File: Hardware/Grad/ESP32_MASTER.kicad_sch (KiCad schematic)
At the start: 35 parts, among them J201 Amphenol 40-Pin FPC, U201 LM66200DRLR, U202 TLV75733PDRV, U203 SN74LVC1G139, U204 ESP32-S3-WROOM-1-N8R8, U205 TC7MBL3126CFT, U206 AP3019AKTTR, U207 W25Q128JVP, U208 THVD1400D

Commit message: Prototype of PCB layout
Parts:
- added C1101, C1104, C1105: 100nF, Capacitor_SMD:C_0402_1005Metric, symbol Device:C_Small_US
- added C1102, C1103, C1106: 22uF, Capacitor_SMD:C_0603_1608Metric, symbol Device:C_Polarized_Small_US
- added D1101, D1102: LED_Small, New_Library:Worthington_LED_0603, symbol Device:LED_Small
- added J101: 6-Pos 2.54mm Header, Connector_PinHeader_2.54mm:PinHeader_1x06_P2.54mm_Vertical_SMD_Pin1Left, symbol Connector_Generic:Conn_01x06
- added J1101: JST-PH SPI, Connector_JST:JST_PH_S5B-PH-K_1x05_P2.00mm_Horizontal, symbol Connector_Generic:Conn_01x05
- added J1102: JST-PH UART/I2C, Connector_JST:JST_PH_S6B-PH-K_1x06_P2.00mm_Horizontal, symbol Connector_Generic:Conn_01x06
- added J1103: JST-PH A#, Connector_JST:JST_PH_S6B-PH-K_1x06_P2.00mm_Horizontal, symbol Connector_Generic:Conn_01x06
- added J1104: Micro_SD_Card, New_Library:CUI_MSD-4-A, symbol Connector:Micro_SD_Card
- added J202, J203, J204, J205: 01x30 Pads, Connector_PinSocket_2.54mm:PinSocket_1x30_P2.54mm_Vertical, symbol Connector_Generic:Conn_01x30
- added J3: 2x8 2.54mm IDC Header, Connector_IDC:IDC-Header_2x06_P2.54mm_Vertical_SMD, symbol Connector_Generic:Conn_02x06_Odd_Even
- added R1101: 1k, New_Library:Worthington_R_0402, symbol Device:R_Small_US
- added R1102: 430, New_Library:Worthington_R_0402, symbol Device:R_Small_US
- added R203, R204: 120, New_Library:Worthington_R_0402, symbol Device:R_Small_US
- added RN1101: 47k, New_Library:RESCAXE80P320X160X70-8N, symbol Libraries:R_Network04_Split
- added U1101: TC7MBL3126CFT, Package_SO:TSSOP-14_4.4x5mm_P0.65mm, symbol Analog_Switch:CD4066BPW
- added U1102: AZ1117-5.0, Package_TO_SOT_SMD:SOT-223-3_TabPin2, symbol Regulator_Linear:AZ1117-5.0
- added U1103: THVD1400D, Package_SO:SOIC-8_3.9x4.9mm_P1.27mm, symbol Interface_UART:THVD1400D
- added U1104: QTPy SAMD21, New_Library:Py_QT_SAMD21, symbol New_Library:QT_Py_SAMD21
- D201: value LED_Small -> RED
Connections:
- net BACKLIGHT_PWM_IN: now also J3.8 (Pin_8)
- net BATT_IN: now also C1102.1, J3.1 (Pin_1), J3.12 (Pin_12), U1102.3 (VI)
- net ESP_PROG_EN: now also J101.2 (Pin_2)
- net ESP_PROG_IO0: now also J101.3 (Pin_3)
- net ESP_PROG_RXD0: now also J101.5 (Pin_5)
- net ESP_PROG_TXD0: now also J101.4 (Pin_4)
- net FRAME_SYNC_IN: now also J3.10 (Pin_10); no longer U204.39 (IO1)
- net GND: now also D202.1 (K), D203.1 (K), D204.1 (K), D205.1 (K), U207.4 (GND), C1101.2, C1102.2, C1103.2, C1104.2, C1105.2, C1106.2, J101.6 (Pin_6), J1101.5 (Pin_5), J1102.6 (Pin_6), J1103.6 (Pin_6), J1104.6 (VSS), J1104.9 (SHIELD), J202.1 (Pin_1), J202.10 (Pin_10), J202.11 (Pin_11), J202.12 (Pin_12), J202.13 (Pin_13), J202.14 (Pin_14), J202.15 (Pin_15), J202.16 (Pin_16), J202.17 (Pin_17), J202.18 (Pin_18), J202.19 (Pin_19), J202.2 (Pin_2), J202.20 (Pin_20), J202.21 (Pin_21), J202.22 (Pin_22), J202.23 (Pin_23), J202.24 (Pin_24), J202.25 (Pin_25), J202.26 (Pin_26), J202.27 (Pin_27), J202.28 (Pin_28), J202.29 (Pin_29), J202.3 (Pin_3), J202.30 (Pin_30), J202.4 (Pin_4), J202.5 (Pin_5), J202.6 (Pin_6), J202.7 (Pin_7), J202.8 (Pin_8), J202.9 (Pin_9), J203.1 (Pin_1), J203.10 (Pin_10), J203.11 (Pin_11), J203.12 (Pin_12), J203.13 (Pin_13), J203.14 (Pin_14), J203.15 (Pin_15), J203.16 (Pin_16), J203.17 (Pin_17), J203.18 (Pin_18), J203.19 (Pin_19), J203.2 (Pin_2), J203.20 (Pin_20), J203.21 (Pin_21), J203.22 (Pin_22), J203.23 (Pin_23), J203.24 (Pin_24), J203.25 (Pin_25), J203.26 (Pin_26), J203.27 (Pin_27), J203.28 (Pin_28), J203.29 (Pin_29), J203.3 (Pin_3), J203.30 (Pin_30), J203.4 (Pin_4), J203.5 (Pin_5), J203.6 (Pin_6), J203.7 (Pin_7), J203.8 (Pin_8), J203.9 (Pin_9), J204.1 (Pin_1), J204.10 (Pin_10), J204.11 (Pin_11), J204.12 (Pin_12), J204.13 (Pin_13), J204.14 (Pin_14), J204.15 (Pin_15), J204.16 (Pin_16), J204.17 (Pin_17), J204.18 (Pin_18), J204.19 (Pin_19), J204.2 (Pin_2), J204.20 (Pin_20), J204.21 (Pin_21), J204.22 (Pin_22), J204.23 (Pin_23), J204.24 (Pin_24), J204.25 (Pin_25), J204.26 (Pin_26), J204.27 (Pin_27), J204.28 (Pin_28), J204.29 (Pin_29), J204.3 (Pin_3), J204.30 (Pin_30), J204.4 (Pin_4), J204.5 (Pin_5), J204.6 (Pin_6), J204.7 (Pin_7), J204.8 (Pin_8), J204.9 (Pin_9), J205.1 (Pin_1), J205.10 (Pin_10), J205.11 (Pin_11), J205.12 (Pin_12), J205.13 (Pin_13), J205.14 (Pin_14), J205.15 (Pin_15), J205.16 (Pin_16), J205.17 (Pin_17), J205.18 (Pin_18), J205.19 (Pin_19), J205.2 (Pin_2), J205.20 (Pin_20), J205.21 (Pin_21), J205.22 (Pin_22), J205.23 (Pin_23), J205.24 (Pin_24), J205.25 (Pin_25), J205.26 (Pin_26), J205.27 (Pin_27), J205.28 (Pin_28), J205.29 (Pin_29), J205.3 (Pin_3), J205.30 (Pin_30), J205.4 (Pin_4), J205.5 (Pin_5), J205.6 (Pin_6), J205.7 (Pin_7), J205.8 (Pin_8), J205.9 (Pin_9), J3.11 (Pin_11), J3.2 (Pin_2), R1101.2, R1102.2, U1101.7 (GND), U1102.1 (GND), U1103.5 (GND), U1104.13 (GND); no longer RN202.5, RN202.6, RN202.7 (5), RN202.8
- net RS485_A: now also J3.4 (Pin_4), R203.1, R204.1, U1103.6 (A)
- net RS485_B: now also J3.6 (Pin_6), R203.2, R204.2, U1103.7 (B)
- net SPI_CS_FLASH: now also RN202.6; no longer D204.2 (A)
- net SPI_CS_LCD: now also RN201.7 (5), RN202.5; no longer D205.2 (A), RN201.5
- net SPI_CS_µSD: now also RN201.5, RN202.7 (5), J1103.3 (Pin_3), J1104.2 (DAT3/CD), J3.3 (Pin_3), RN1101.5, U1101.11 (B4), U1101.12 (A4), U1104.2 (A1); no longer D203.2 (A), RN201.7 (5)
- net SPI_MISO_µSD: now also J1104.7 (DAT0), J3.9 (Pin_9), RN1101.7 (5), U1101.2 (A1)
- net SPI_MOSI_µSD: now also J1104.3 (CMD), J3.7 (Pin_7), RN1101.6, U1101.6 (B2)
- net SPI_SCK_µSD: now also J1104.5 (CLK), J3.5 (Pin_5), RN1101.8, U1101.8 (B3)
- net SPI_µSD_BUS_CONNECT: now also RN202.8, J1103.2 (Pin_2), U1101.1 (1~{OE}), U1101.10 (3~{OE}), U1101.13 (4~{OE}), U1101.4 (2~{OE}), U1104.1 (A0); no longer D202.2 (A)
- net UART-RS485_RX: now also J1102.5 (Pin_5), U1103.1 (RO), U1104.8 (RX)
- net UART-RS485_TX: now also J1102.4 (Pin_4), U1103.4 (DI), U1104.7 (TX)
- net UART_RS485_DE: now also J1103.5 (Pin_5), U1103.2 (~{RE}), U1103.3 (DE), U1104.4 (A3)
- net at RN202.1 (4): now also D202.2 (A); no longer D202.1 (K)
- net at RN202.4: now also D205.2 (A); no longer D205.1 (K)
- net at RN202.3: now also D204.2 (A); no longer D204.1 (K)
- net at RN202.2: now also D203.2 (A); no longer D203.1 (K)
- net PROG_PWR_IN renamed ESP_PROG_PWR
- net ESP_PROG_PWR: now also J101.1 (Pin_1)
- new net: D1101.1 (K), R1101.1
- new net: D1102.1 (K), R1102.1
- new net BACKLIGHT_PWM: J1102.3 (Pin_3), U1104.6 (SCL)
- new net FRAME_SYNC: J1103.4 (Pin_4), U1104.3 (A2), U204.39 (IO1)
- new net SAMD21_3V3: C1101.1, C1105.1, C1106.1, D1102.2 (A), J1104.4 (VDD), RN1101.1 (4), RN1101.2, RN1101.3, RN1101.4, U1101.14 (VCC), U1103.8 (VCC), U1104.12 (3V)
- new net SAMD21_5V: C1103.1, C1104.1, D1101.2 (A), J1101.1 (Pin_1), J1102.1 (Pin_1), J1103.1 (Pin_1), U1102.2 (VO), U1104.14 (5V)
- new net SAMD_MISO: J1101.3 (Pin_3), U1101.3 (B1), U1104.10 (MI)
- new net SAMD_MOSI: J1101.4 (Pin_4), U1101.5 (A2), U1104.11 (MO)
- new net SAMD_SCK: J1101.2 (Pin_2), U1101.9 (A3), U1104.9 (SCK)
- new net SAMD_SDA: J1102.2 (Pin_2), U1104.5 (SDA)
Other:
- note added: "Populate 120R Resistor If Last Panel In Chain"
- note added: "QTPy SAMD21 has +5V -> +3V3 Regulator Onboard "3V" Pin is the output from this regulator"
- moved on the sheet: C201, C202, C203, C204, C205, C206, C207, C208, C209, C210, C211, C212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

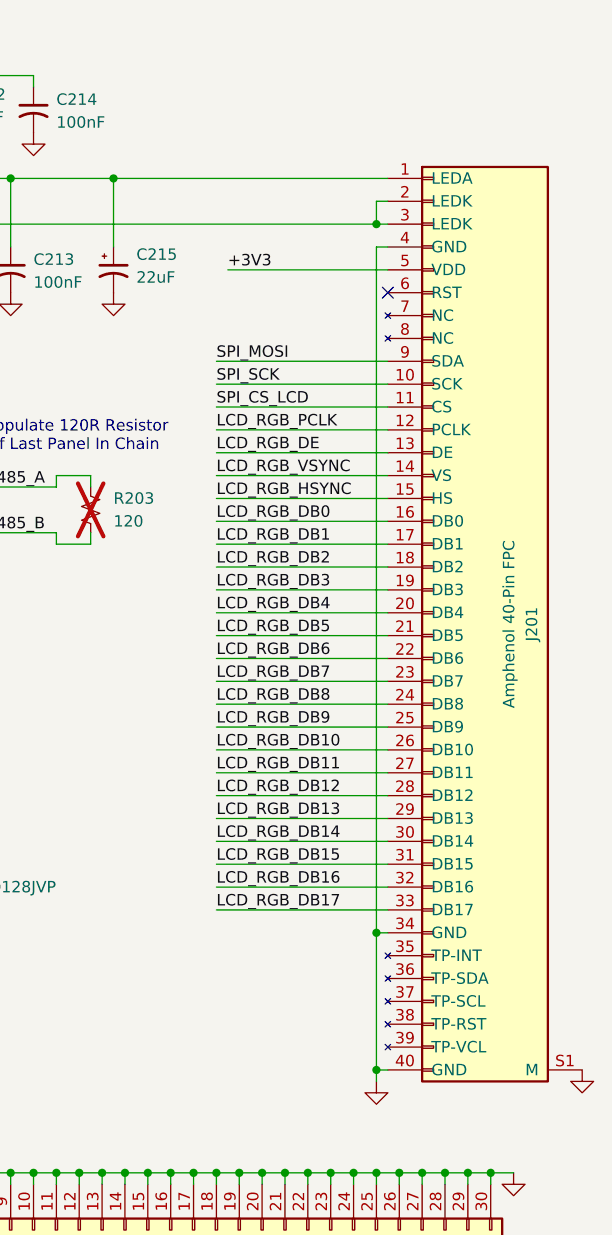
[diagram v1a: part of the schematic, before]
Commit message: Fixed flipped FPC connector pinout
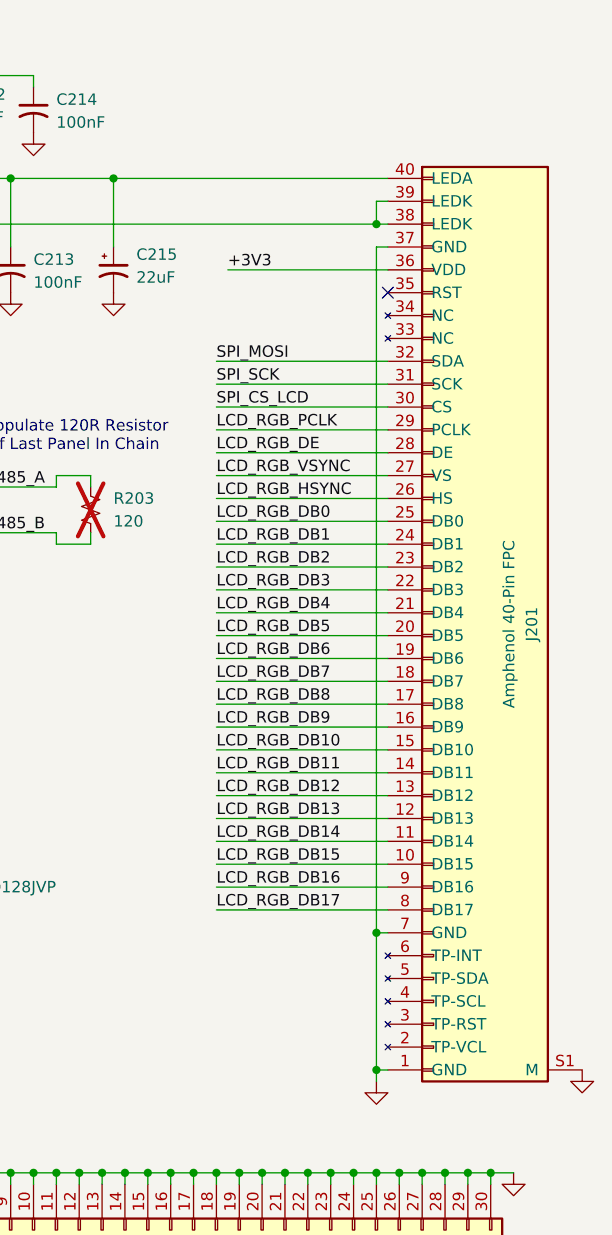
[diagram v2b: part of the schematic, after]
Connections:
- net +3V3: now also J201.36 (VDD); no longer J201.5 (VDD)
- net GND: now also J201.1 (GND), J201.37 (GND), J201.7 (GND); no longer J201.34 (GND), J201.4 (GND), J201.40 (GND)
- net LCD_RGB_DB0: now also J201.25 (DB0); no longer J201.16 (DB0)
- net LCD_RGB_DB1: now also J201.24 (DB1); no longer J201.17 (DB1)
- net LCD_RGB_DB10: now also J201.15 (DB10); no longer J201.26 (DB10)
- net LCD_RGB_DB11: now also J201.14 (DB11); no longer J201.27 (DB11)
- net LCD_RGB_DB12: now also J201.13 (DB12); no longer J201.28 (DB12)
- net LCD_RGB_DB13: now also J201.12 (DB13); no longer J201.29 (DB13)
- net LCD_RGB_DB14: now also J201.11 (DB14); no longer J201.30 (DB14)
- net LCD_RGB_DB15: now also J201.10 (DB15); no longer J201.31 (DB15)
- net LCD_RGB_DB16: now also J201.9 (DB16); no longer J201.32 (DB16)
- net LCD_RGB_DB17: now also J201.8 (DB17); no longer J201.33 (DB17)
- net LCD_RGB_DB2: now also J201.23 (DB2); no longer J201.18 (DB2)
- net LCD_RGB_DB3: now also J201.22 (DB3); no longer J201.19 (DB3)
- net LCD_RGB_DB4: now also J201.21 (DB4); no longer J201.20 (DB4)
- net LCD_RGB_DB5: now also J201.20 (DB5); no longer J201.21 (DB5)
- net LCD_RGB_DB6: now also J201.19 (DB6); no longer J201.22 (DB6)
- net LCD_RGB_DB7: now also J201.18 (DB7); no longer J201.23 (DB7)
- net LCD_RGB_DB8: now also J201.17 (DB8); no longer J201.24 (DB8)
- net LCD_RGB_DB9: now also J201.16 (DB9); no longer J201.25 (DB9)
- net LCD_RGB_DE: now also J201.28 (DE); no longer J201.13 (DE)
- net LCD_RGB_HSYNC: now also J201.26 (HS); no longer J201.15 (HS)
- net LCD_RGB_PCLK: now also J201.29 (PCLK); no longer J201.12 (PCLK)
- net LCD_RGB_VSYNC: now also J201.27 (VS); no longer J201.14 (VS)
- net SPI_CS_LCD: now also J201.30 (CS); no longer J201.11 (CS)
- net SPI_MOSI: now also J201.32 (SDA); no longer J201.9 (SDA)
- net SPI_SCK: now also J201.31 (SCK); no longer J201.10 (SCK)
- net at C213.1, C215.1, U206.5 (V_{OUT}): now also J201.40 (LEDA); no longer J201.1 (LEDA)
- net at R202.1, U206.3 (FB): now also J201.38 (LEDK), J201.39 (LEDK); no longer J201.2 (LEDK), J201.3 (LEDK)

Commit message: More routing progress
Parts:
- added C223: 22uF, Capacitor_SMD:C_0603_1608Metric, symbol Device:C_Polarized_Small_US
- added D207: RED, New_Library:Worthington_LED_0603, symbol Device:LED_Small
- added J101: Power In, Connector_JST:JST_PH_S2B-PH-K_1x02_P2.00mm_Horizontal, symbol Connector_Generic:Conn_01x02
- added J211: SPI TestPoint, Connector_PinHeader_2.54mm:PinHeader_1x06_P2.54mm_Vertical_SMD_Pin1Left, symbol Connector_Generic:Conn_01x06
- added R104, R105: 10, Resistor_SMD:R_1210_3225Metric, symbol Device:R_Small_US
- added R208: 1k, New_Library:Worthington_R_0402, symbol Device:R_Small_US
- added RN204: 10k, New_Library:RESCAXE80P320X160X70-8N, symbol Libraries:R_Network04_Split
- D206: renamed from D1101; value LED_Small -> RED
- D208: renamed from D1102; value LED_Small -> RED
- J207: renamed from J1101; value JST-PH SPI -> SPI TestPoint; footprint Connector_JST:JST_PH_S5B-PH-K_1x05_P2.00mm_Horizontal -> Connector_PinHeader_2.54mm:PinHeader_1x06_P2.54mm_Vertical_SMD_Pin1Left; symbol Connector_Generic:Conn_01x05 -> Connector_Generic:Conn_01x06
- J208: renamed from J1102; value JST-PH UART/I2C -> RS485 TestPoint; footprint Connector_JST:JST_PH_S6B-PH-K_1x06_P2.00mm_Horizontal -> Connector_PinHeader_2.54mm:PinHeader_1x05_P2.54mm_Vertical_SMD_Pin1Left; symbol Connector_Generic:Conn_01x06 -> Connector_Generic:Conn_01x05
- J209: renamed from J1103; value JST-PH A# -> Extra TestPoint; footprint Connector_JST:JST_PH_S6B-PH-K_1x06_P2.00mm_Horizontal -> Connector_PinHeader_2.54mm:PinHeader_1x05_P2.54mm_Vertical_SMD_Pin1Left; symbol Connector_Generic:Conn_01x06 -> Connector_Generic:Conn_01x05
- U211: renamed from U1102; footprint Package_TO_SOT_SMD:SOT-223-3_TabPin2 -> Package_TO_SOT_SMD:SOT-89-3
- renumbered C201 to C101, C202 to C102, C203 to C103, C206 to C104, C208 to C105, C210 to C106, C204 to C107, C205 to C108, C207 to C109, C209 to C110, C211 to C111, C216 to C112, C212 to C113, C213 to C114, C214 to C115, C215 to C116, C1101 to C217, C1102 to C218, C1103 to C219, C1104 to C220, C1105 to C221, C1106 to C222, D201 to D101, D202 to D102, D203 to D103, D204 to D104, D205 to D105, J101 to J102, J3 to J103, J201 to J104, J1104 to J210, J202 to J401, J204 to J402, J205 to J403, J203 to J404, L201 to L101, R201 to R101, R202 to R102, R203 to R103, R1101 to R207, R1102 to R209, RN201 to RN101, RN202 to RN102, RN1101 to RN203, U201 to U101, U202 to U102, U203 to U103, U204 to U104, U205 to U105, U206 to U106, U208 to U107, U207 to U108, U1101 to U209, U1103 to U210, U1104 to U212
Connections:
- net BACKLIGHT_PWM_IN is gone; now on net BACKLIGHT_PWM: J103.8 (Pin_8), U106.4 (CTRL)
- net FRAME_SYNC_IN is gone; now on net FRAME_SYNC: J103.10 (Pin_10)
- net BACKLIGHT_PWM: now also J209.4 (Pin_4); no longer J208.3 (Pin_3)
- net BATT_IN: now also J401.25 (Pin_25), J401.26 (Pin_26), J401.5 (Pin_5), J401.6 (Pin_6), J402.25 (Pin_25), J402.26 (Pin_26), J402.5 (Pin_5), J402.6 (Pin_6), J403.25 (Pin_25), J403.26 (Pin_26), J403.5 (Pin_5), J403.6 (Pin_6), J404.25 (Pin_25), J404.26 (Pin_26), J404.5 (Pin_5), J404.6 (Pin_6), J101.1 (Pin_1); no longer J103.1 (Pin_1), J103.12 (Pin_12)
- net FRAME_SYNC: now also J209.3 (Pin_3); no longer J209.4 (Pin_4)
- net GND: now also J103.1 (Pin_1), J103.12 (Pin_12), J207.1 (Pin_1), J207.6 (Pin_6), J208.1 (Pin_1), J208.5 (Pin_5), J209.1 (Pin_1), J209.5 (Pin_5), C223.2, J101.2 (Pin_2), J211.2 (Pin_2), J211.4 (Pin_4), J211.6 (Pin_6); no longer J207.5 (Pin_5), J208.6 (Pin_6), J209.6 (Pin_6), J401.25 (Pin_25), J401.26 (Pin_26), J401.5 (Pin_5), J401.6 (Pin_6), J402.25 (Pin_25), J402.26 (Pin_26), J402.5 (Pin_5), J402.6 (Pin_6), J403.25 (Pin_25), J403.26 (Pin_26), J403.5 (Pin_5), J403.6 (Pin_6), J404.1 (Pin_1), J404.10 (Pin_10), J404.11 (Pin_11), J404.12 (Pin_12), J404.13 (Pin_13), J404.14 (Pin_14), J404.15 (Pin_15), J404.16 (Pin_16), J404.17 (Pin_17), J404.18 (Pin_18), J404.19 (Pin_19), J404.2 (Pin_2), J404.20 (Pin_20), J404.21 (Pin_21), J404.22 (Pin_22), J404.23 (Pin_23), J404.24 (Pin_24), J404.25 (Pin_25), J404.26 (Pin_26), J404.3 (Pin_3), J404.4 (Pin_4), J404.5 (Pin_5), J404.6 (Pin_6), J404.7 (Pin_7), J404.8 (Pin_8), J404.9 (Pin_9)
- net SAMD21_3V3: now also C223.1, D207.2 (A), RN204.1 (4)
- net SAMD21_5V: no longer J207.1 (Pin_1), J208.1 (Pin_1), J209.1 (Pin_1)
- net SPI_CS_µSD: no longer J103.3 (Pin_3), J209.3 (Pin_3), J210.2 (DAT3/CD), RN203.5, U209.11 (B4), U209.12 (A4), U212.2 (A1)
- net SPI_MISO_µSD: no longer J103.9 (Pin_9), J210.7 (DAT0), RN203.7 (5), U209.2 (A1)
- net SPI_MOSI_µSD: no longer J103.7 (Pin_7), J210.3 (CMD), RN203.6, U209.6 (B2)
- net SPI_SCK_µSD: no longer J103.5 (Pin_5), J210.5 (CLK), RN203.8, U209.8 (B3)
- net SPI_µSD_BUS_CONNECT: no longer J209.2 (Pin_2), U212.1 (A0)
- net UART-RS485_RX: no longer J208.5 (Pin_5), U212.8 (RX)
- net UART-RS485_TX: no longer J208.4 (Pin_4), U212.7 (TX)
- net UART_RS485_DE: no longer J209.5 (Pin_5), U212.4 (A3)
- net at R102.1, U106.3 (FB): now also R104.1, R105.1; no longer J104.38 (LEDK), J104.39 (LEDK)
- net at J210.CD (CHIP_DETECT): now also R208.2
- net SAMD_SDA renamed SAMD_UART-RS485_DE
- new net: J211.3 (Pin_3), RN204.3, RN204.7 (5)
- new net: J211.5 (Pin_5), RN204.6
- new net: J104.39 (LEDK), R105.2
- new net: J104.38 (LEDK), R104.2
- new net: J404.1 (Pin_1), J404.10 (Pin_10), J404.11 (Pin_11), J404.12 (Pin_12), J404.13 (Pin_13), J404.14 (Pin_14), J404.15 (Pin_15), J404.16 (Pin_16), J404.17 (Pin_17), J404.18 (Pin_18), J404.19 (Pin_19), J404.2 (Pin_2), J404.20 (Pin_20), J404.21 (Pin_21), J404.22 (Pin_22), J404.23 (Pin_23), J404.24 (Pin_24), J404.3 (Pin_3), J404.4 (Pin_4), J404.7 (Pin_7), J404.8 (Pin_8), J404.9 (Pin_9)
- new net: D207.1 (K), R208.1
- new net BUTTON_SENSE: J211.1 (Pin_1), RN204.2, RN204.8, U212.4 (A3)
- new net SAMD_CS_µSD: J207.5 (Pin_5), U209.12 (A4), U212.2 (A1)
- new net SAMD_UART-RS485_RX: J208.4 (Pin_4), U212.8 (RX)
- new net SAMD_UART-RS485_TX: J208.3 (Pin_3), U212.7 (TX)
- new net SAMD_µSD_BUS_CONNECT: J209.2 (Pin_2), U212.1 (A0)
- new net µSD_SPI_CS: J103.3 (Pin_3), J210.2 (DAT3/CD), RN203.5, U209.11 (B4)
- new net µSD_SPI_MISO: J103.9 (Pin_9), J210.7 (DAT0), RN203.7 (5), U209.2 (A1)
- new net µSD_SPI_MOSI: J103.7 (Pin_7), J210.3 (CMD), RN203.6, U209.6 (B2)
- new net µSD_SPI_SCK: J103.5 (Pin_5), J210.5 (CLK), RN203.8, U209.8 (B3)
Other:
- moved on the sheet: C221, C222, D208, R103, R204, R209, U212
